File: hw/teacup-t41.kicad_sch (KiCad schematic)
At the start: 104 parts, among them IC1 T41NQ, J1 USB Type-C, J10 AudioJack4_Ground, J11 Conn_01x04_Pin, J12 Conn_01x04_Pin, J13 SFW15R-2STE1LF, J14 Conn_01x02_MountingPin, J15 Conn_01x03_MountingPin, J16 Conn_01x03_MountingPin, J2 Micro_SD_Card, J3 USB_A, J4 Conn_02x08_Odd_Even, J5 UART, J6 Conn_02x07_Odd_Even, J7 Conn_02x07_Odd_Even, J8 DC_IN, J9 Conn_01x02_MountingPin, SW2 SW_SPDT, U1 AZ1117-3.3, U2 AZ1117-1.8, U3 MCP1826S, U4 W25Q32JVSS, U5 W25Q32JVSS, Y1 24 MHz

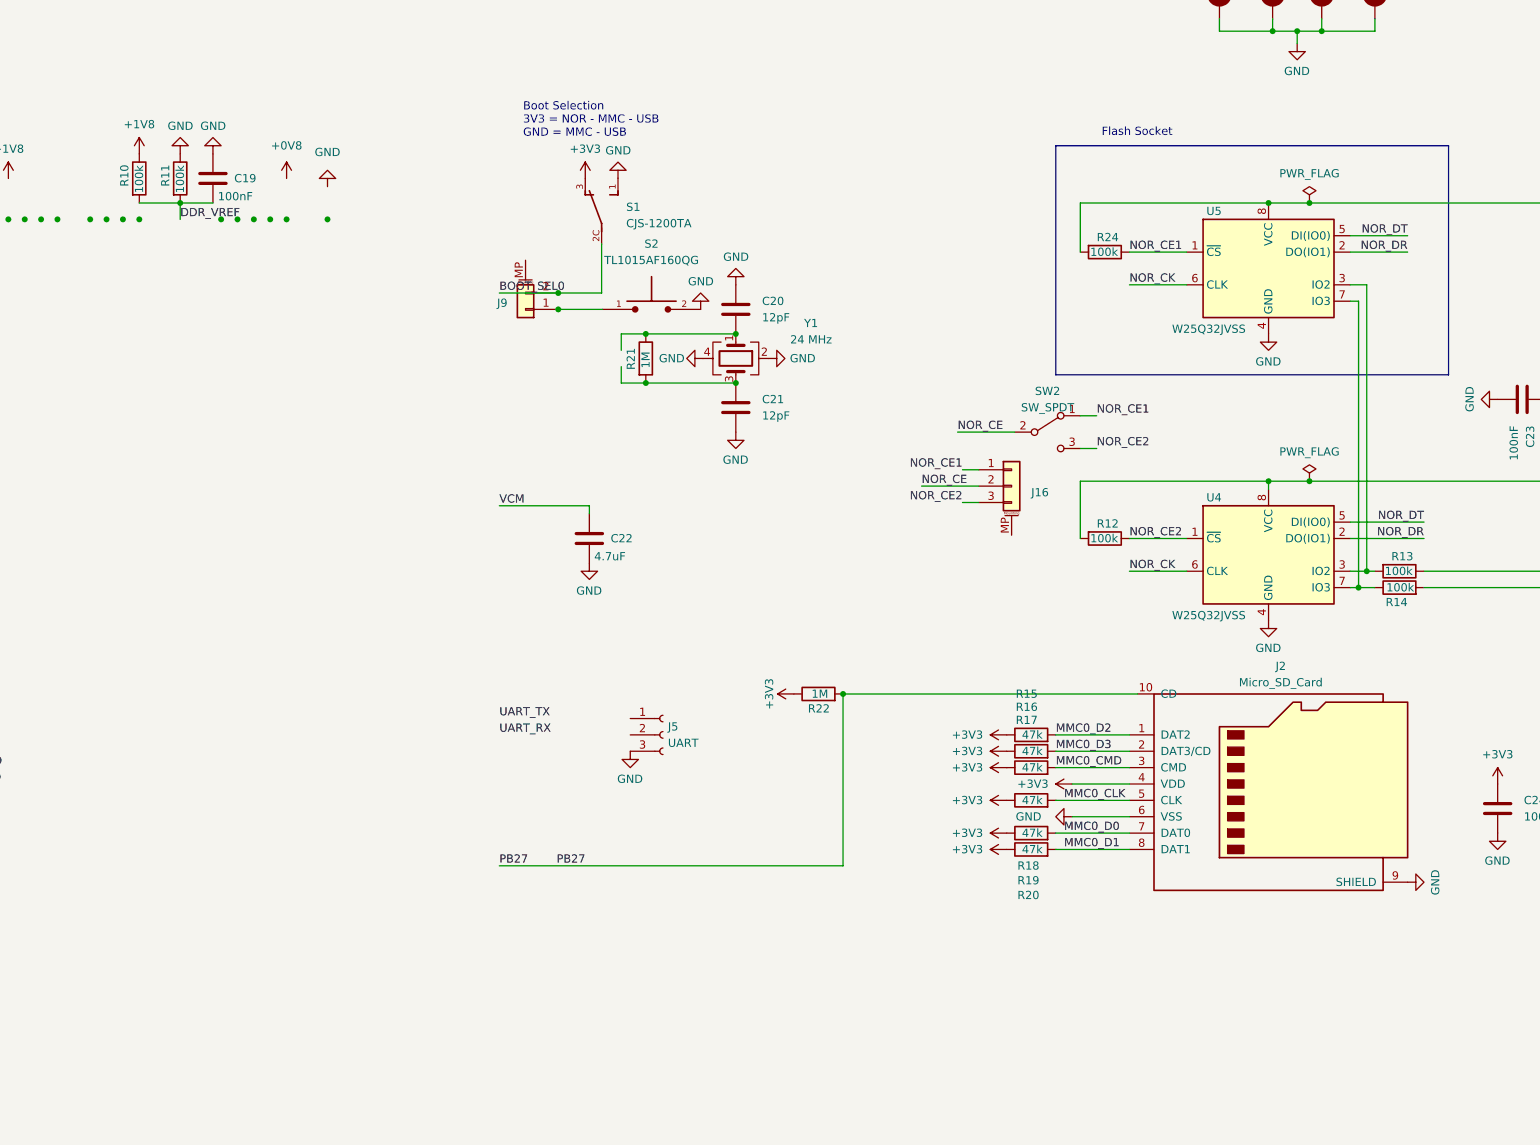
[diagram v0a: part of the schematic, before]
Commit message: Add T41 new circuits: DDR ZQ, POR strap, MICNL, NOR quad, VREF retarget
R26/R27 240R ZQ->GND, R28 1K POR_CTL->+3V3, C47 100nF MICNL->GND,
NOR_WP/NOR_HOLD tie SFC IO2/IO3 to flash (quad), VREF divider top
retargeted +1V8->+1V35 (0.675V). Netlist re-verified: new nets
connect, IC1 still 0 mismatch. Remaining: power bucks (+0V8 core,
+1V35 DDR undriven), orphan cleanup (S2/J9 PPRST).
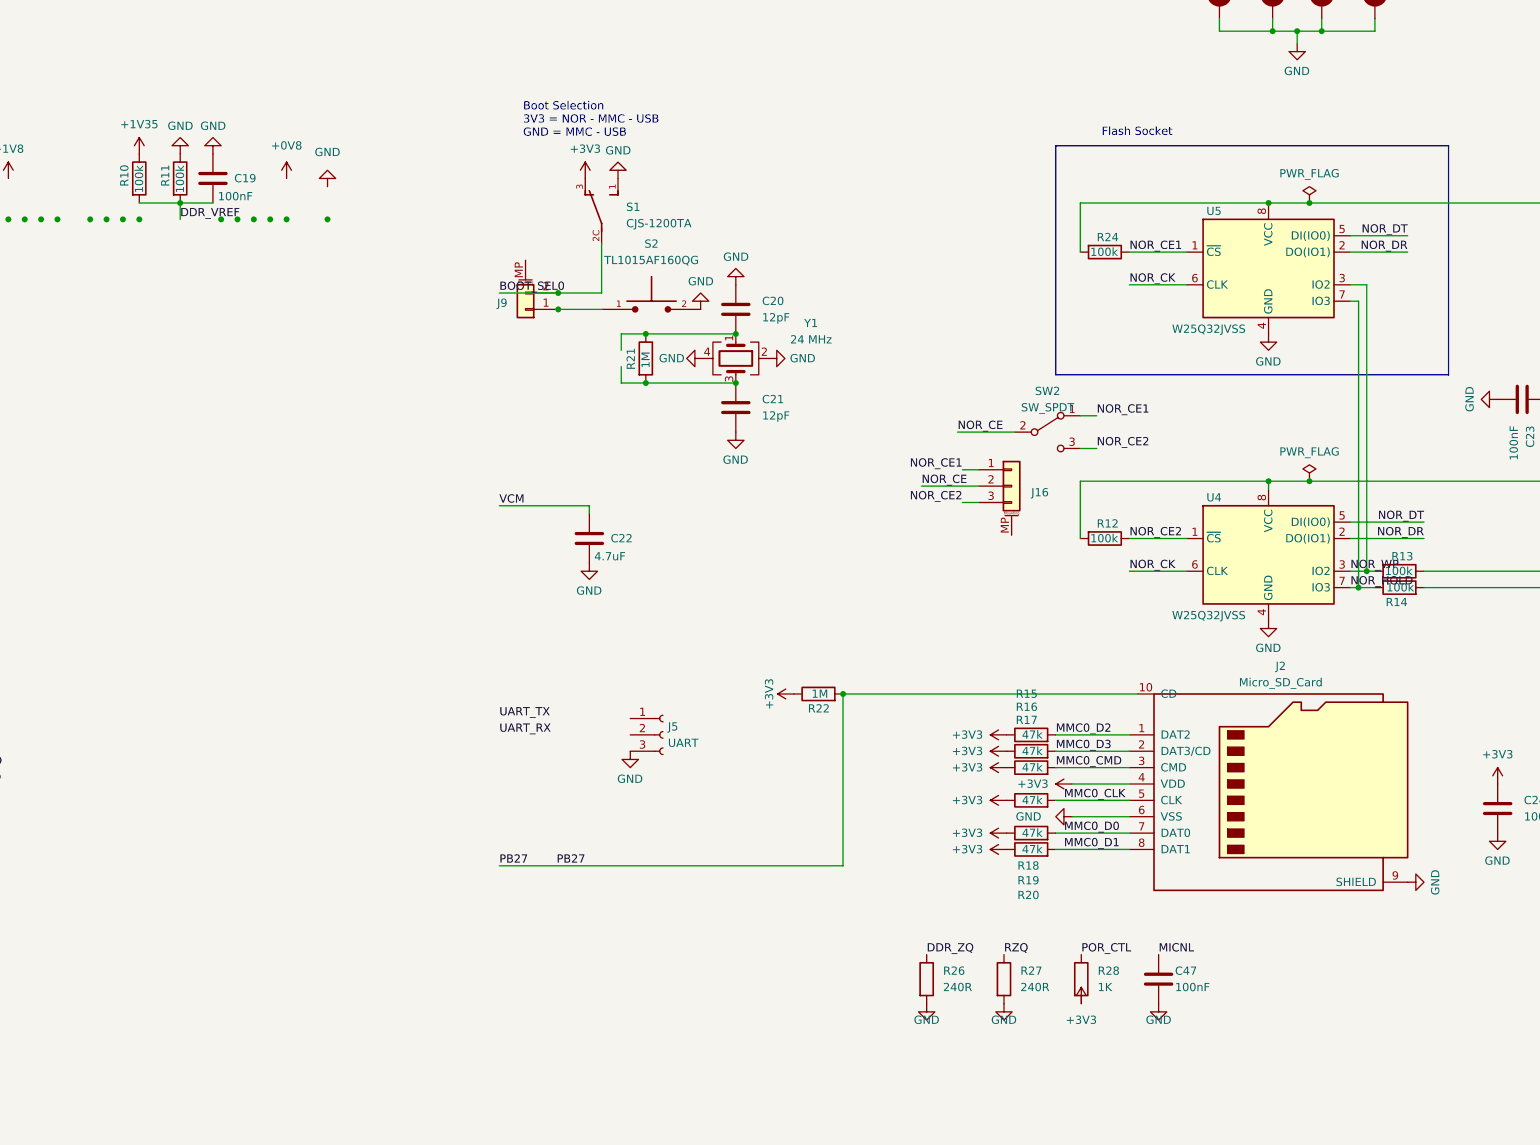
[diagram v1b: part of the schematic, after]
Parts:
- added C47: 100nF, C_0402_1005Metric, symbol Device:C
- added R26, R27: 240R, R_0603_1608Metric_Pad0.98x0.95mm_HandSolder, symbol Device:R
- added R28: 1K, R_0603_1608Metric_Pad0.98x0.95mm_HandSolder, symbol Device:R
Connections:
- net +1V35: now also R10.1
- net +1V8: no longer R10.1
- net +3V3: now also R28.2
- net DDR_ZQ: now also R26.1
- net GND: now also C47.2, R26.2, R27.2
- net MICNL: now also C47.1
- net NOR_HOLD: now also R14.1, U4.7 (IO3), U5.7 (IO3)
- net NOR_WP: now also R13.2, U4.3 (IO2), U5.3 (IO2)
- net POR_CTL: now also R28.1
- net RZQ: now also R27.1
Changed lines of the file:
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@@
     )
   )
-  (symbol (lib_id "power:+1V8") (at 177.8 121.92 0) (unit 1)
+  (symbol (lib_id "teacup:+1V35") (at 177.8 121.92 0) (unit 1)
     (in_bom yes) (on_board yes) (dnp no) (fields_autoplaced)
     (property "Reference" "#PWR015" (at 177.8 125.73 0)
       (effects (font (size 1.27 1.27)) hide)
     )
-    (property "Value" "+1V8" (at 177.8 117.348 0)
+    (property "Value" "+1V35" (at 177.8 117.348 0)
       (effects (font (size 1.27 1.27)))
     )
@@
         (path "/6e7ef4e6-2026-4726-8de0-60238113f775" (reference "#PWR149") (unit 1))))
   )
+  (symbol (lib_id "Device:R") (at 300 250 0) (unit 1)
+    (in_bom yes) (on_board yes) (dnp no)
+    (property "Reference" "R26" (at 302.54 248.73 0) (effects (font (size 1.27 1.27)) (justify left)))
+    (property "Value" "240R" (at 302.54 251.27 0) (effects (font (size 1.27 1.27)) (justify left)))
+    (property "Footprint" "R_0603_1608Metric_Pad0.98x0.95mm_HandSolder" (at 300 250 0) (effects (font (size 1.27 1.27)) hide))
+    (pin "1") (pin "2")
+    (instances (project "teacup-t41" (path "/6e7ef4e6-2026-4726-8de0-60238113f775" (reference "R26") (unit 1)))))
+  (label "DDR_ZQ" (at 300 246.19 0)
+    (effects (font (size 1.27 1.27)) (justify left bottom)))
+  (symbol (lib_id "power:GND") (at 300 253.81 0) (unit 1)
+    (in_bom yes) (on_board yes) (dnp no)
+    (property "Reference" "#PWR150" (at 300 251.27 0) (effects (font (size 1.27 1.27)) hide))
+    (property "Value" "GND" (at 300 256.35 0) (effects (font (size 1.27 1.27))))
+    (pin "1")
+    (instances (project "teacup-t41" (path "/6e7ef4e6-2026-4726-8de0-60238113f775" (reference "#PWR150") (unit 1)))))
+  (symbol (lib_id "Device:R") (at 312 250 0) (unit 1)
+    (in_bom yes) (on_board yes) (dnp no)
+    (property "Reference" "R27" (at 314.54 248.73 0) (effects (font (size 1.27 1.27)) (justify left)))
+    (property "Value" "240R" (at 314.54 251.27 0) (effects (font (size 1.27 1.27)) (justify left)))
+    (property "Footprint" "R_0603_1608Metric_Pad0.98x0.95mm_HandSolder" (at 312 250 0) (effects (font (size 1.27 1.27)) hide))
+    (pin "1") (pin "2")
+    (instances (project "teacup-t41" (path "/6e7ef4e6-2026-4726-8de0-60238113f775" (reference "R27") (unit 1)))))
+  (label "RZQ" (at 312 246.19 0)
+    (effects (font (size 1.27 1.27)) (justify left bottom)))
+  (symbol (lib_id "power:GND") (at 312 253.81 0) (unit 1)
+    (in_bom yes) (on_board yes) (dnp no)
+    (property "Reference" "#PWR151" (at 312 251.27 0) (effects (font (size 1.27 1.27)) hide))
+    (property "Value" "GND" (at 312 256.35 0) (effects (font (size 1.27 1.27))))
+    (pin "1")
+    (instances (project "teacup-t41" (path "/6e7ef4e6-2026-4726-8de0-60238113f775" (reference "#PWR151") (unit 1)))))
+  (symbol (lib_id "Device:R") (at 324 250 0) (unit 1)
+    (in_bom yes) (on_board yes) (dnp no)
+    (property "Reference" "R28" (at 326.54 248.73 0) (effects (font (size 1.27 1.27)) (justify left)))
+    (property "Value" "1K" (at 326.54 251.27 0) (effects (font (size 1.27 1.27)) (justify left)))
+    (property "Footprint" "R_0603_1608Metric_Pad0.98x0.95mm_HandSolder" (at 324 250 0) (effects (font (size 1.27 1.27)) hide))
+    (pin "1") (pin "2")
+    (instances (project "teacup-t41" (path "/6e7ef4e6-2026-4726-8de0-60238113f775" (reference "R28") (unit 1)))))
+  (label "POR_CTL" (at 324 246.19 0)
+    (effects (font (size 1.27 1.27)) (justify left bottom)))
+  (symbol (lib_id "power:+3V3") (at 324 253.81 0) (unit 1)
+    (in_bom yes) (on_board yes) (dnp no)
+    (property "Reference" "#PWR152" (at 324 251.27 0) (effects (font (size 1.27 1.27)) hide))
+    (property "Value" "+3V3" (at 324 256.35 0) (effects (font (size 1.27 1.27))))
+    (pin "1")
+    (instances (project "teacup-t41" (path "/6e7ef4e6-2026-4726-8de0-60238113f775" (reference "#PWR152") (unit 1)))))
+  (symbol (lib_id "Device:C") (at 336 250 0) (unit 1)
+    (in_bom yes) (on_board yes) (dnp no)
+    (property "Reference" "C47" (at 338.54 248.73 0) (effects (font (size 1.27 1.27)) (justify left)))
+    (property "Value" "100nF" (at 338.54 251.27 0) (effects (font (size 1.27 1.27)) (justify left)))
+    (property "Footprint" "C_0402_1005Metric" (at 336 250 0) (effects (font (size 1.27 1.27)) hide))
+    (pin "1") (pin "2")
+    (instances (project "teacup-t41" (path "/6e7ef4e6-2026-4726-8de0-60238113f775" (reference "C47") (unit 1)))))
+  (label "MICNL" (at 336 246.19 0)
+    (effects (font (size 1.27 1.27)) (justify left bottom)))
+  (symbol (lib_id "power:GND") (at 336 253.81 0) (unit 1)
+    (in_bom yes) (on_board yes) (dnp no)
+    (property "Reference" "#PWR153" (at 336 251.27 0) (effects (font (size 1.27 1.27)) hide))
+    (property "Value" "GND" (at 336 256.35 0) (effects (font (size 1.27 1.27))))
+    (pin "1")
+    (instances (project "teacup-t41" (path "/6e7ef4e6-2026-4726-8de0-60238113f775" (reference "#PWR153") (unit 1)))))
+  (label "NOR_WP" (at 365.76 186.69 0)
+    (effects (font (size 1.27 1.27)) (justify left bottom)))
+  (label "NOR_HOLD" (at 365.76 189.23 0)
+    (effects (font (size 1.27 1.27)) (justify left bottom)))
   (sheet_instances
     (path "/" (page "1"))

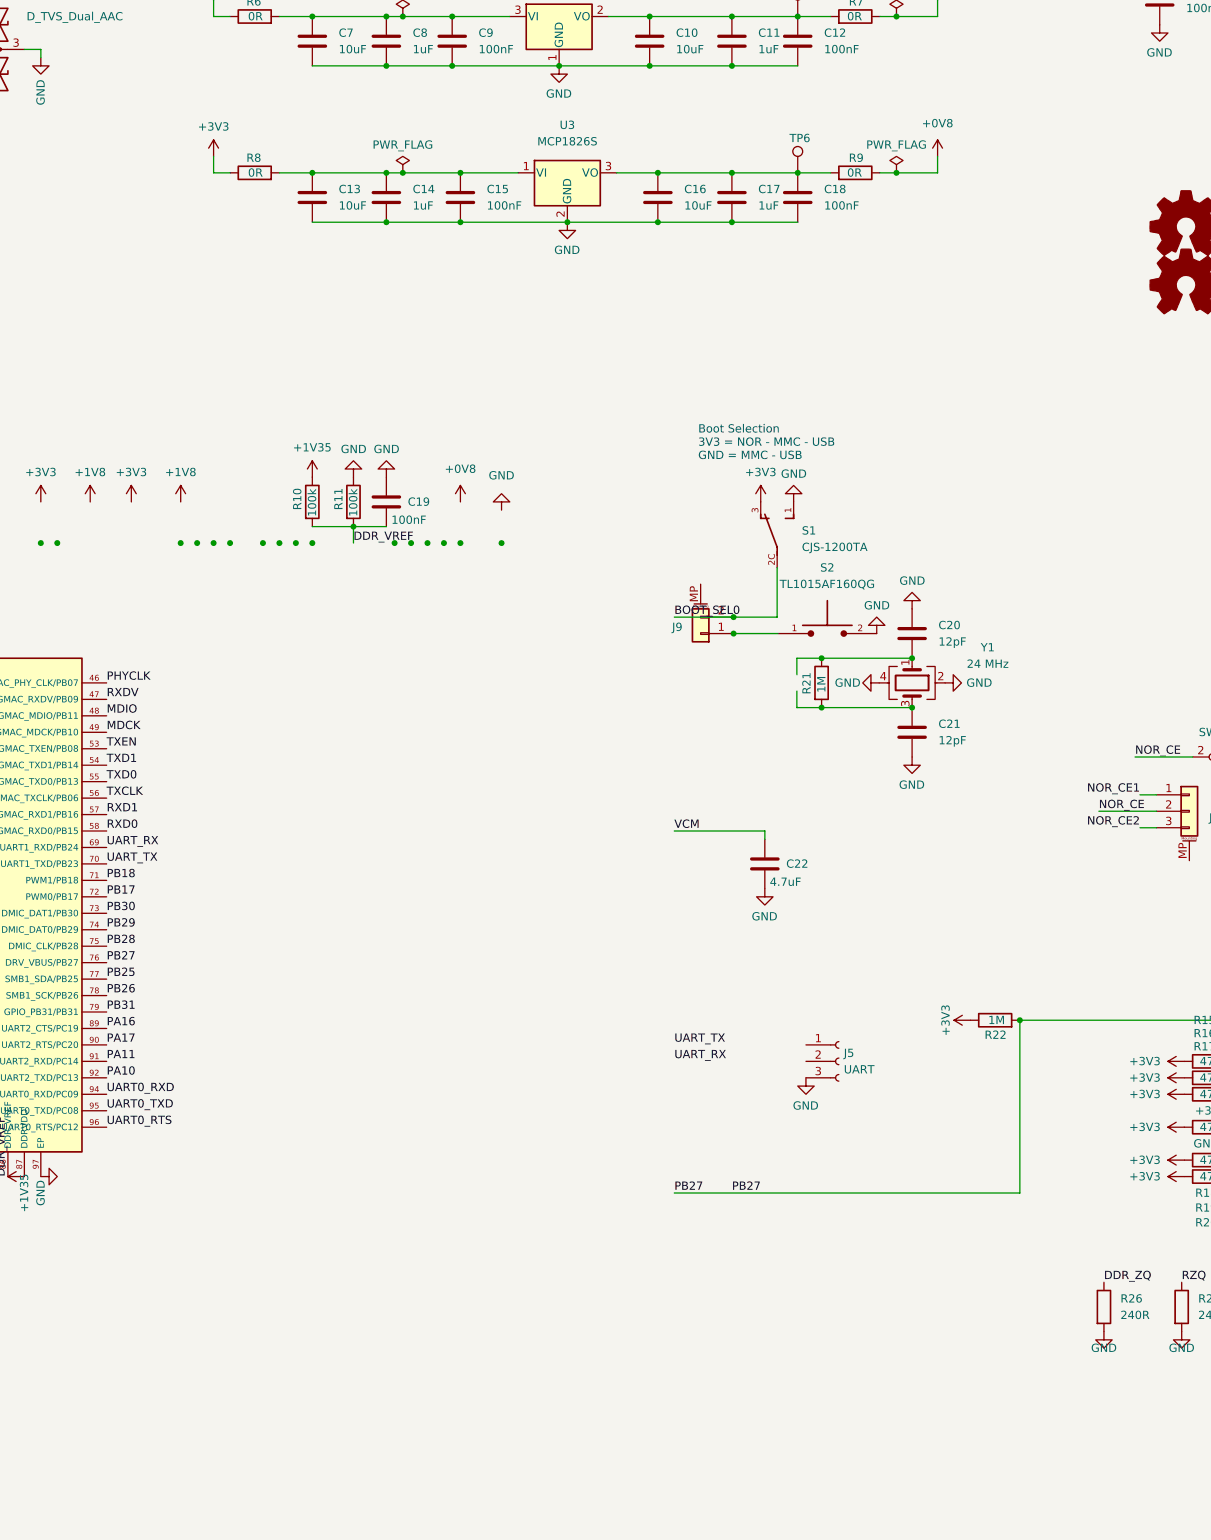
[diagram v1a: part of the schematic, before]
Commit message: Add T41 power bucks (core 0.8V, DDR 1.35V); schematic complete
U6 SY8089 buck +0V8 2A (EN<-1V35, FB 100k/300k), U7 SY8089 buck +1V35
(EN<-1V8, FB 150k/120k), L1/L2 2.2uH, in/out caps + feedforward.
Removed U3 (MCP1826S, insufficient 1A core LDO); kept AZ1117 3V3/1V8.
EN cascade gives DS 6.6.1 order. New SY8089 + Device:L symbols.

Netlist re-verified: IC1 0 mismatch, all 103 components have footprints.
Remaining ERC items (orphan power ports, dangling stub fragments,
off-grid, lib-mismatch) are cosmetic - no PCB effect; GUI-polish before
fab. gen_power_bucks.py in scripts/.
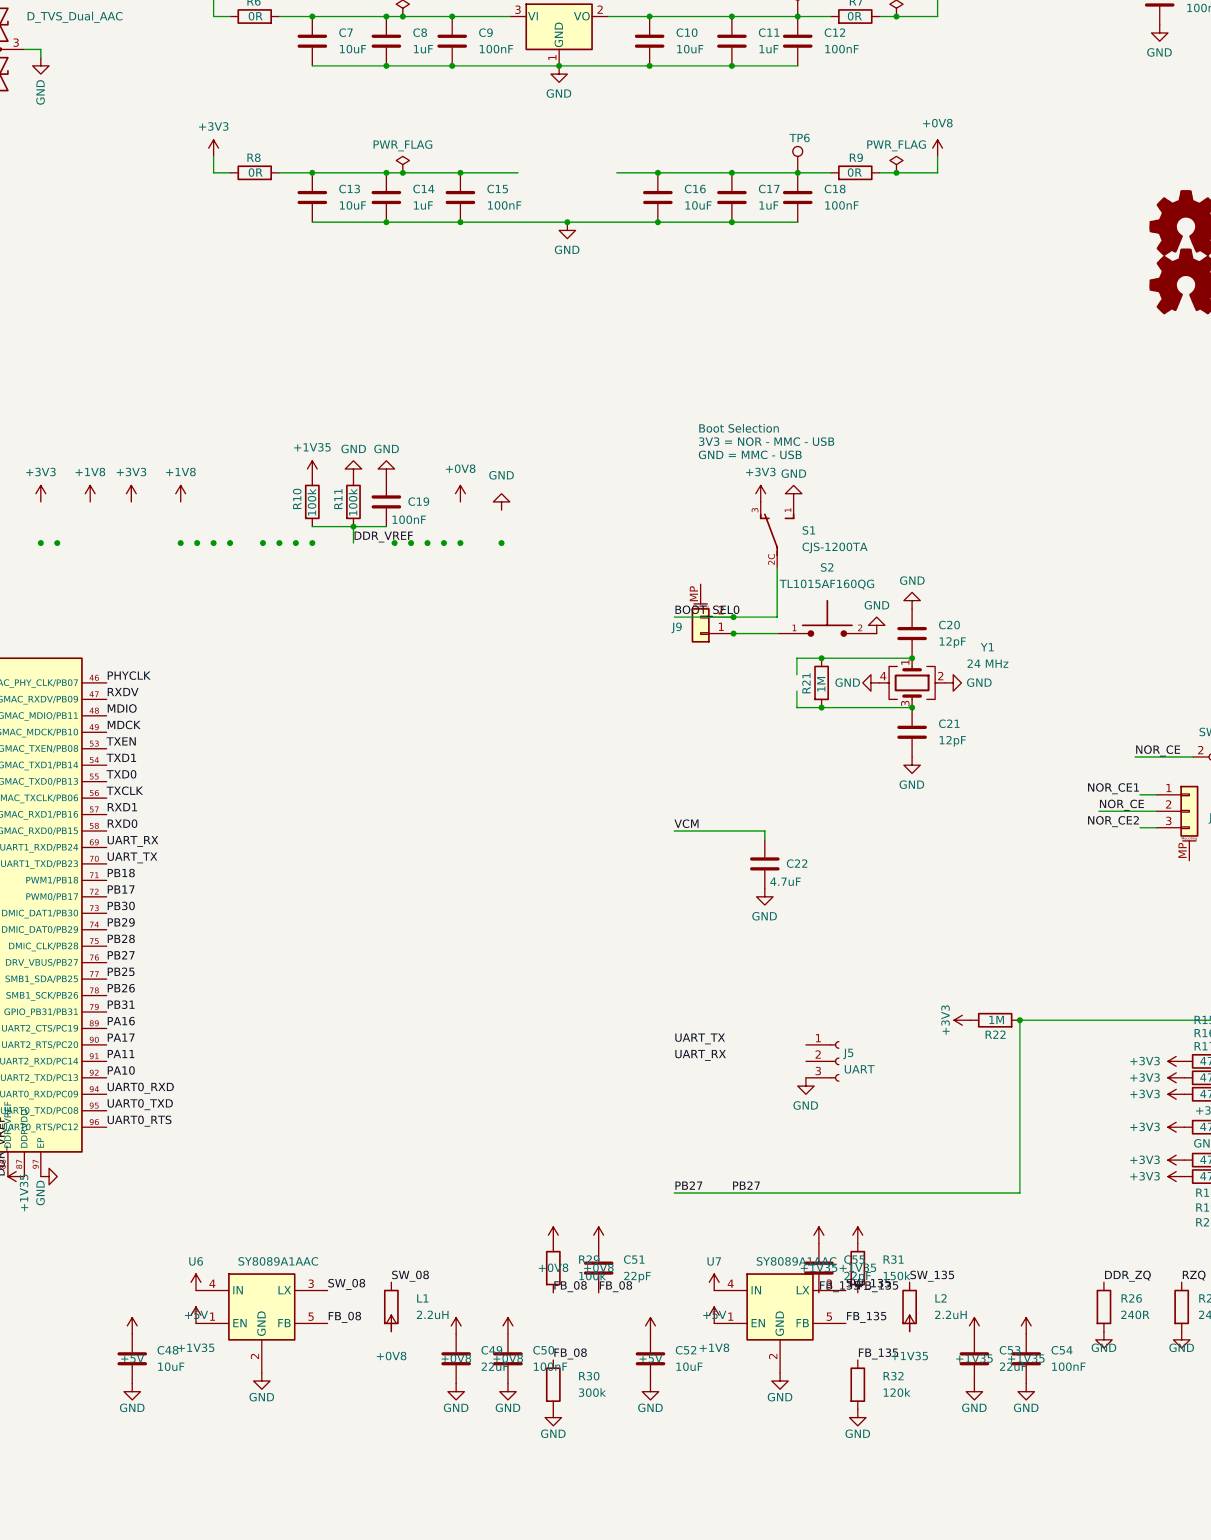
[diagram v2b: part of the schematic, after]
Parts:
- removed U3: MCP1826S, Package_TO_SOT_SMD:SOT-223-3_TabPin2, symbol Regulator_Linear:MCP1826S
- added C48, C52: 10uF, C_0805_2012Metric_Pad1.18x1.45mm_HandSolder, symbol Device:C
- added C49, C53: 22uF, C_0805_2012Metric_Pad1.18x1.45mm_HandSolder, symbol Device:C
- added C50, C54: 100nF, C_0402_1005Metric, symbol Device:C
- added C51, C55: 22pF, C_0402_1005Metric, symbol Device:C
- added L1, L2: 2.2uH, Inductor_SMD:L_1210_3225Metric, symbol Device:L
- added R29: 100k, R_0402_1005Metric, symbol Device:R
- added R30: 300k, R_0402_1005Metric, symbol Device:R
- added R31: 150k, R_0402_1005Metric, symbol Device:R
- added R32: 120k, R_0402_1005Metric, symbol Device:R
- added U6, U7: SY8089A1AAC, Package_TO_SOT_SMD:SOT-23-5, symbol teacup:SY8089
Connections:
- net +0V8: now also C49.1, C50.1, C51.1, L1.2, R29.1
- net +1V35: now also C53.1, C54.1, C55.1, L2.2, R31.1, U6.1 (EN)
- net +1V8: now also U7.1 (EN)
- net +5V: now also C48.1, C52.1, U6.4 (IN), U7.4 (IN)
- net GND: now also C48.2, C49.2, C50.2, C52.2, C53.2, C54.2, R30.2, R32.2, U6.2 (GND), U7.2 (GND)
- new net FB_08: C51.2, R29.2, R30.1, U6.5 (FB)
- new net FB_135: C55.2, R31.2, R32.1, U7.5 (FB)
- new net SW_08: L1.1, U6.3 (LX)
- new net SW_135: L2.1, U7.3 (LX)
